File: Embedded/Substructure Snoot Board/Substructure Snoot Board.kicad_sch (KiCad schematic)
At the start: 31 parts, among them J1 D0 FFC, J2 D1 FFC, J3 L0 JST, J4 L1 JST, J5 XT30, U1 D0 FFC, U2 D1 FFC, U3 U FFC, U4 S FFC, U5 R FFC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

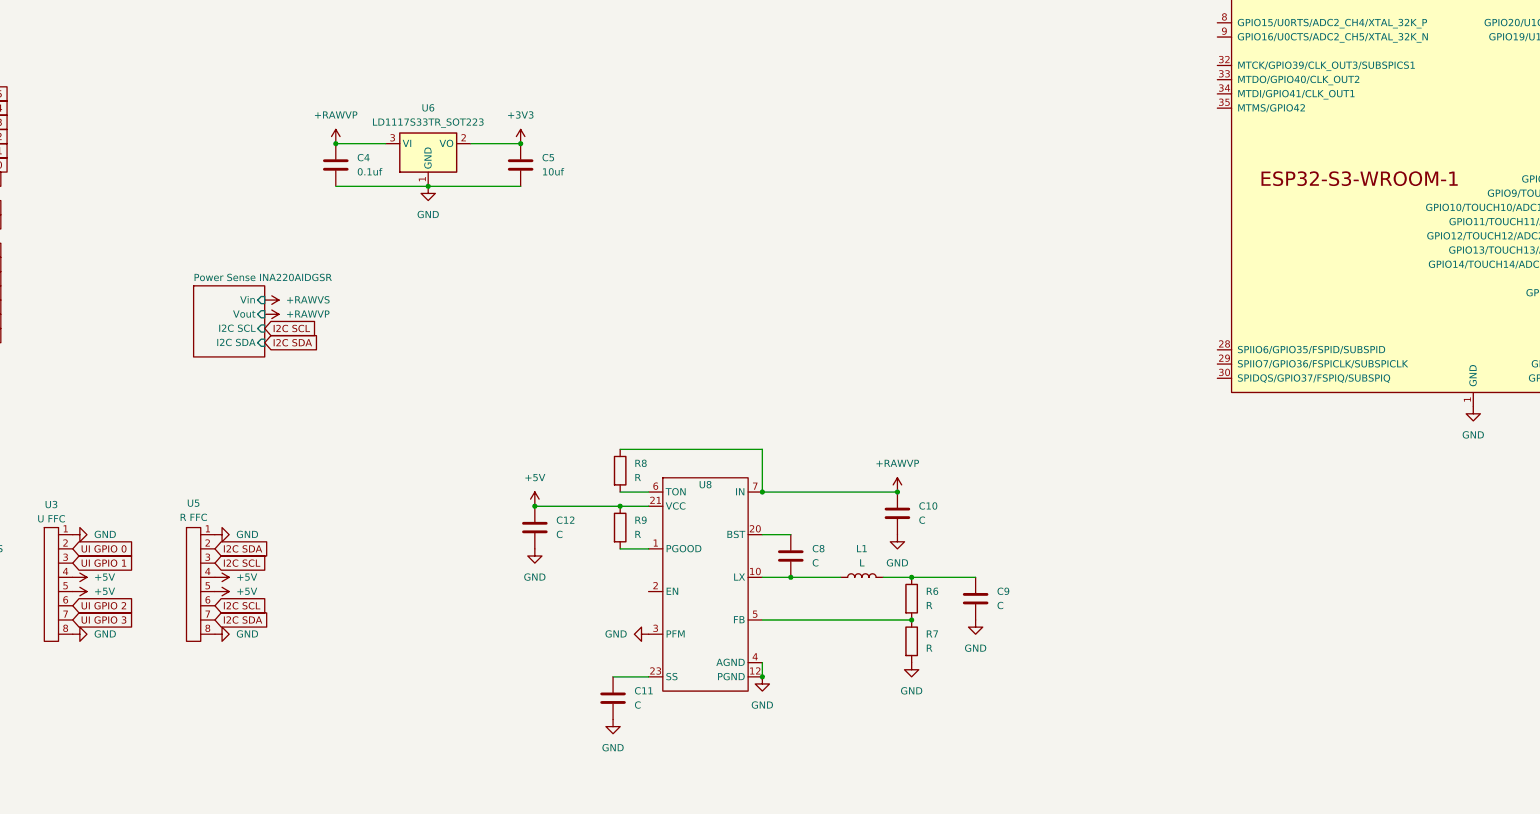
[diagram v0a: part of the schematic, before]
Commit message: Added AOZ2264QI Component Values (Basic Running)
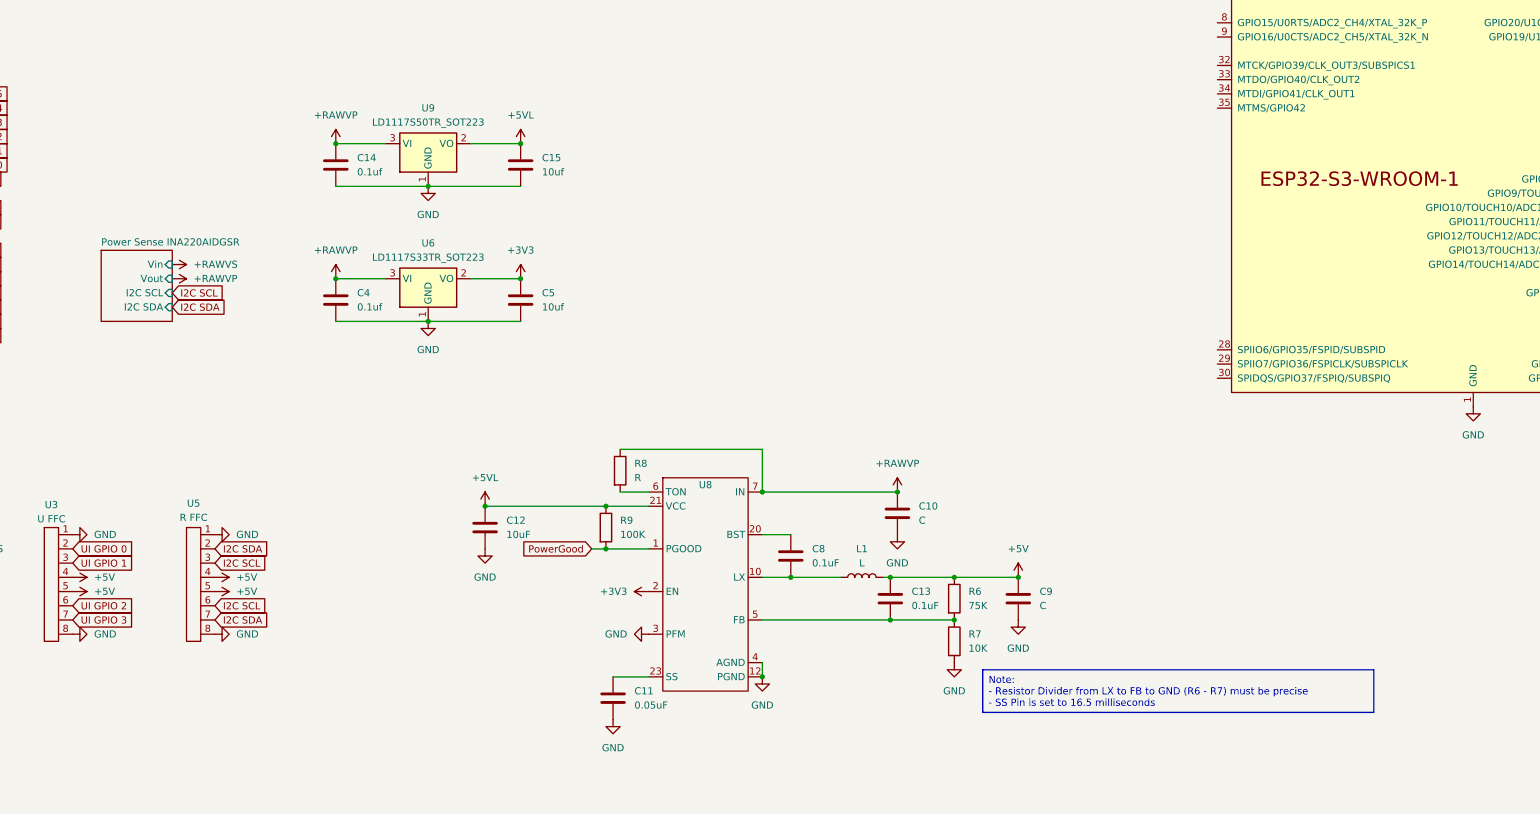
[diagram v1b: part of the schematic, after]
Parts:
- added C13: 0.1uF, symbol Device:C
- added C14: 0.1uf, Capacitor_SMD:C_0402_1005Metric_Pad0.74x0.62mm_HandSolder, symbol Device:C
- added C15: 10uf, Capacitor_SMD:C_0402_1005Metric_Pad0.74x0.62mm_HandSolder, symbol Device:C
- added U9: LD1117S50TR_SOT223, Package_TO_SOT_SMD:SOT-223-3_TabPin2, symbol Regulator_Linear:LD1117S50TR_SOT223
- C11: value C -> 0.05uF
- C12: value C -> 10uF
- C8: value C -> 0.1uF
- R6: value R -> 75K
- R7: value R -> 10K
- R9: value R -> 100K
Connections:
- net +3V3: now also U8.2 (EN)
- net +5V: now also C9.1, L1.2, R6.1, C13.1; no longer C12.1, R9.1, U8.21 (VCC)
- net +RAWVP: now also C14.1, U9.3 (VI)
- net GND: now also C14.2, C15.2, U9.1 (GND)
- net PowerGood: now reaches R9.2, U8.1 (PGOOD)
- net at R6.2, R7.1, U8.5 (FB): now also C13.2
- new net +5VL: C12.1, C15.1, R9.1, U8.21 (VCC), U9.2 (VO)
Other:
- moved on the sheet: C12, C4, C5, C9, R6, R7, R9, U6

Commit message: Added Rton Value
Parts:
- C11, C12, C13, C8, R6, R7, R9: footprint (none) -> Resistor_SMD:R_0402_1005Metric_Pad0.72x0.64mm_HandSolder
- R8: value R -> 360K; footprint (none) -> Resistor_SMD:R_0402_1005Metric_Pad0.72x0.64mm_HandSolder
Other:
- moved on the sheet: R8
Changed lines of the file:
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@@
 	(wire
 		(pts
-			(xy 177.8 130.81) (xy 203.2 130.81)
+			(xy 175.26 130.81) (xy 203.2 130.81)
 		)
 		(stroke
@@
 	(wire
 		(pts
-			(xy 177.8 138.43) (xy 182.88 138.43)
+			(xy 175.26 138.43) (xy 182.88 138.43)
 		)
 		(stroke
@@
 		)
 	)
-	(text_box "Note:\n- Resistor Divider from LX to FB to GND (R6 - R7) must be precise\n- SS Pin is set to 16.5 milliseconds"
+	(text_box "Note:\n- Resistor Divider from LX to FB to GND (R6 - R7) must be precise\n- SS Pin is set to 16.5 milliseconds\n- Rton Set to 100khz"
 		(exclude_from_sim no)
 		(at 242.57 170.18 0)
-		(size 69.85 7.62)
-		(stroke
-			(width 0)
-			(type default)
-		)
-		(fill
-			(type none)
-		)
-		(effects
-			(font
-				(size 1.27 1.27)
-			)
-			(justify left top)
-		)
-	)
-	(text_box "To Do List\n- Add 5V Power Reg"
-		(exclude_from_sim no)
-		(at 17.78 19.05 0)
-		(size 22.86 5.08)
+		(size 69.85 10.16)
 		(stroke
 			(width 0)
@@
 			)
 		)
-		(property "Footprint" ""
+		(property "Footprint" "Resistor_SMD:R_0402_1005Metric_Pad0.72x0.64mm_HandSolder"
 			(at 209.2452 153.67 0)
 			(effects
@@
 			)
 		)
-		(property "Footprint" ""
+		(property "Footprint" "Resistor_SMD:R_0402_1005Metric_Pad0.72x0.64mm_HandSolder"
 			(at 177.4952 179.07 0)
 			(effects
@@
 			)
 		)
-		(property "Footprint" ""
+		(property "Footprint" "Resistor_SMD:R_0402_1005Metric_Pad0.72x0.64mm_HandSolder"
 			(at 235.712 157.48 90)
 			(effects
@@
 	(symbol
 		(lib_id "Device:R")
-		(at 177.8 134.62 0)
+		(at 175.26 134.62 0)
 		(unit 1)
 		(exclude_from_sim no)
@@
 		(fields_autoplaced yes)
 		(property "Reference" "R8"
-			(at 180.34 133.3499 0)
+			(at 177.8 133.3499 0)
 			(effects
 				(font
@@
 			)
 		)
-		(property "Value" "R"
-			(at 180.34 135.8899 0)
+		(property "Value" "360K"
+			(at 177.8 135.8899 0)
 			(effects
 				(font
@@
 			)
 		)
-		(property "Footprint" ""
-			(at 176.022 134.62 90)
+		(property "Footprint" "Resistor_SMD:R_0402_1005Metric_Pad0.72x0.64mm_HandSolder"
+			(at 173.482 134.62 90)
 			(effects
 				(font
@@
 		)
 		(property "Datasheet" "~"
-			(at 177.8 134.62 0)
+			(at 175.26 134.62 0)
 			(effects
 				(font
@@
 		)
 		(property "Description" "Resistor"
-			(at 177.8 134.62 0)
+			(at 175.26 134.62 0)
 			(effects
 				(font
@@
 			)
 		)
-		(property "Footprint" ""
+		(property "Footprint" "Resistor_SMD:R_0402_1005Metric_Pad0.72x0.64mm_HandSolder"
 			(at 173.482 144.78 90)
 			(effects
@@
 			)
 		)
-		(property "Footprint" ""
+		(property "Footprint" "Resistor_SMD:R_0402_1005Metric_Pad0.72x0.64mm_HandSolder"
 			(at 235.712 165.1 90)
 			(effects
@@
 			)
 		)
-		(property "Footprint" ""
+		(property "Footprint" "Resistor_SMD:R_0402_1005Metric_Pad0.72x0.64mm_HandSolder"
 			(at 154.6352 148.59 0)
 			(effects
@@
 			)
 		)
-		(property "Footprint" ""
+		(property "Footprint" "Resistor_SMD:R_0402_1005Metric_Pad0.72x0.64mm_HandSolder"
 			(at 227.0252 161.29 0)
 			(effects

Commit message: Modified GPU PSU Buck Converter IC to LM5176PWPR
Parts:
- removed C10, C9: C, symbol Device:C
- removed C11: 0.05uF, Resistor_SMD:R_0402_1005Metric_Pad0.72x0.64mm_HandSolder, symbol Device:C
- removed C12: 10uF, Resistor_SMD:R_0402_1005Metric_Pad0.72x0.64mm_HandSolder, symbol Device:C
- removed C13, C8: 0.1uF, Resistor_SMD:R_0402_1005Metric_Pad0.72x0.64mm_HandSolder, symbol Device:C
- removed L1: L, symbol Device:L
- removed R6: 75K, Resistor_SMD:R_0402_1005Metric_Pad0.72x0.64mm_HandSolder, symbol Device:R
- removed R7: 10K, Resistor_SMD:R_0402_1005Metric_Pad0.72x0.64mm_HandSolder, symbol Device:R
- removed R8: 360K, Resistor_SMD:R_0402_1005Metric_Pad0.72x0.64mm_HandSolder, symbol Device:R
- removed R9: 100K, Resistor_SMD:R_0402_1005Metric_Pad0.72x0.64mm_HandSolder, symbol Device:R
- removed U8: ~, Power Regulator:AOZ2264QI, symbol Power Regulator:AOZ2264QI
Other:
- added sheet Buck Converter (buckconverter.kicad_sch)

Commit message: Added Buck Converter Components
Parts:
- removed C14: 0.1uf, Capacitor_SMD:C_0402_1005Metric_Pad0.74x0.62mm_HandSolder, symbol Device:C
- removed C15: 10uf, Capacitor_SMD:C_0402_1005Metric_Pad0.74x0.62mm_HandSolder, symbol Device:C
- removed U9: LD1117S50TR_SOT223, Package_TO_SOT_SMD:SOT-223-3_TabPin2, symbol Regulator_Linear:LD1117S50TR_SOT223

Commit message: Added Buck Converter Component Values
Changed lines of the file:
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@@
 		)
 	)
+	(text_box "To Do List\n- Buck Converter Values\n- Buck Converter Footprints\n- Overall Component Placement"
+		(exclude_from_sim no)
+		(at 19.05 19.05 0)
+		(size 34.29 10.16)
+		(stroke
+			(width 0)
+			(type default)
+		)
+		(fill
+			(type none)
+		)
+		(effects
+			(font
+				(size 1.27 1.27)
+			)
+			(justify left top)
+		)
+	)
 	(global_label "Disp GPIO 6"
 		(shape input)
@@
 	(symbol
 		(lib_id "power:+5VP")
-		(at 165.1 154.94 90)
+		(at 127 66.04 90)
 		(unit 1)
 		(exclude_from_sim no)
@@
 		(fields_autoplaced yes)
 		(property "Reference" "#PWR054"
-			(at 168.91 154.94 0)
+			(at 130.81 66.04 0)
 			(effects
 				(font
@@
 		)
 		(property "Value" "+RAWVS"
-			(at 161.29 154.9399 90)
+			(at 123.19 66.0399 90)
 			(effects
 				(font
@@
 		)
 		(property "Footprint" ""
-			(at 165.1 154.94 0)
+			(at 127 66.04 0)
 			(effects
 				(font
@@
 		)
 		(property "Datasheet" ""
-			(at 165.1 154.94 0)
+			(at 127 66.04 0)
 			(effects
 				(font
@@
 		)
 		(property "Description" "Power symbol creates a global label with name \"+5VP\""
-			(at 165.1 154.94 0)
+			(at 127 66.04 0)
 			(effects
 				(font
@@
 	(symbol
 		(lib_id "power:+5V")
-		(at 196.85 154.94 270)
+		(at 158.75 66.04 270)
 		(unit 1)
 		(exclude_from_sim no)
@@
 		(fields_autoplaced yes)
 		(property "Reference" "#PWR057"
-			(at 193.04 154.94 0)
+			(at 154.94 66.04 0)
 			(effects
 				(font
@@
 		)
 		(property "Value" "+5V"
-			(at 200.66 154.9399 90)
+			(at 162.56 66.0399 90)
 			(effects
 				(font
@@
 		)
 		(property "Footprint" ""
-			(at 196.85 154.94 0)
+			(at 158.75 66.04 0)
 			(effects
 				(font
@@
 		)
 		(property "Datasheet" ""
-			(at 196.85 154.94 0)
+			(at 158.75 66.04 0)
 			(effects
 				(font
@@
 		)
 		(property "Description" "Power symbol creates a global label with name \"+5V\""
-			(at 196.85 154.94 0)
+			(at 158.75 66.04 0)
 			(effects
 				(font
@@
 	)
 	(sheet
-		(at 165.1 152.4)
+		(at 127 63.5)
 		(size 31.75 5.08)
 		(fields_autoplaced yes)
@@
 		)
 		(property "Sheetname" "Buck Converter"
-			(at 165.1 151.6884 0)
+			(at 127 62.7884 0)
 			(effects
 				(font
@@
 		)
 		(property "Sheetfile" "buckconverter.kicad_sch"
-			(at 165.1 158.0646 0)
+			(at 127 69.1646 0)
 			(effects
 				(font
@@
 		)
 		(pin "Power Output" input
-			(at 196.85 154.94 0)
+			(at 158.75 66.04 0)
 			(effects
 				(font
@@
 		)
 		(pin "Power Input" input
-			(at 165.1 154.94 180)
+			(at 127 66.04 180)
 			(effects
 				(font

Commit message: Added Footprints to the Input Power Filtering (Buck Converter)
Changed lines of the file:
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@@
 		)
 	)
-	(text_box "To Do List\n- Buck Converter Values\n- Buck Converter Footprints\n- Overall Component Placement"
+	(text_box "To Do List\n- Buck Converter Footprints\n- Overall Component Placement"
 		(exclude_from_sim no)
 		(at 19.05 19.05 0)
-		(size 34.29 10.16)
+		(size 34.29 7.62)
 		(stroke
 			(width 0)

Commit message: Added Buck Converter PCB Basic Layout
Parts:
- C4: LCSC (none) -> C155422
- C5: LCSC (none) -> C408132
- U6: LCSC (none) -> C86781

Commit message: Modified Component Placement for Implementation Ideation
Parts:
- J5: footprint Connector_AMASS:AMASS_XT30U-M_1x02_P5.0mm_Vertical -> Connector_AMASS:AMASS_XT30PW-M_1x02_P2.50mm_Horizontal
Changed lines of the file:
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@@
 			)
 		)
-		(property "Footprint" "Connector_AMASS:AMASS_XT30U-M_1x02_P5.0mm_Vertical"
+		(property "Footprint" "Connector_AMASS:AMASS_XT30PW-M_1x02_P2.50mm_Horizontal"
 			(at 50.8 146.05 0)
 			(effects
